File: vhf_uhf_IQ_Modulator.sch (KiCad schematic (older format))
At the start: 28 parts

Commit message: Adding docks and details in diagram
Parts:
- added C? (x2): 10uF 16V, symbol CP_Small
- added C? (x2): CP_Small, symbol CP_Small
- added C? (x4): 2200pF, symbol C_Small
- added J?: Audio-Jack-3, symbol Audio-Jack-3
- added R? (x4): 1K, symbol R
- added RV? (x2): 4k7, symbol POT
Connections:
- wire segments 74 -> 107
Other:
- note added: "1200pF / fc= 132KHz\n2200pF / fc=72KHz\n3300pF / fc=48KHz\n4700pF / fc=34KHz"
- note added: "27dBm 500 mW (max)"
- note added: "Check Volatge"
- moved on the sheet: C?, F?, J?, R?, U?

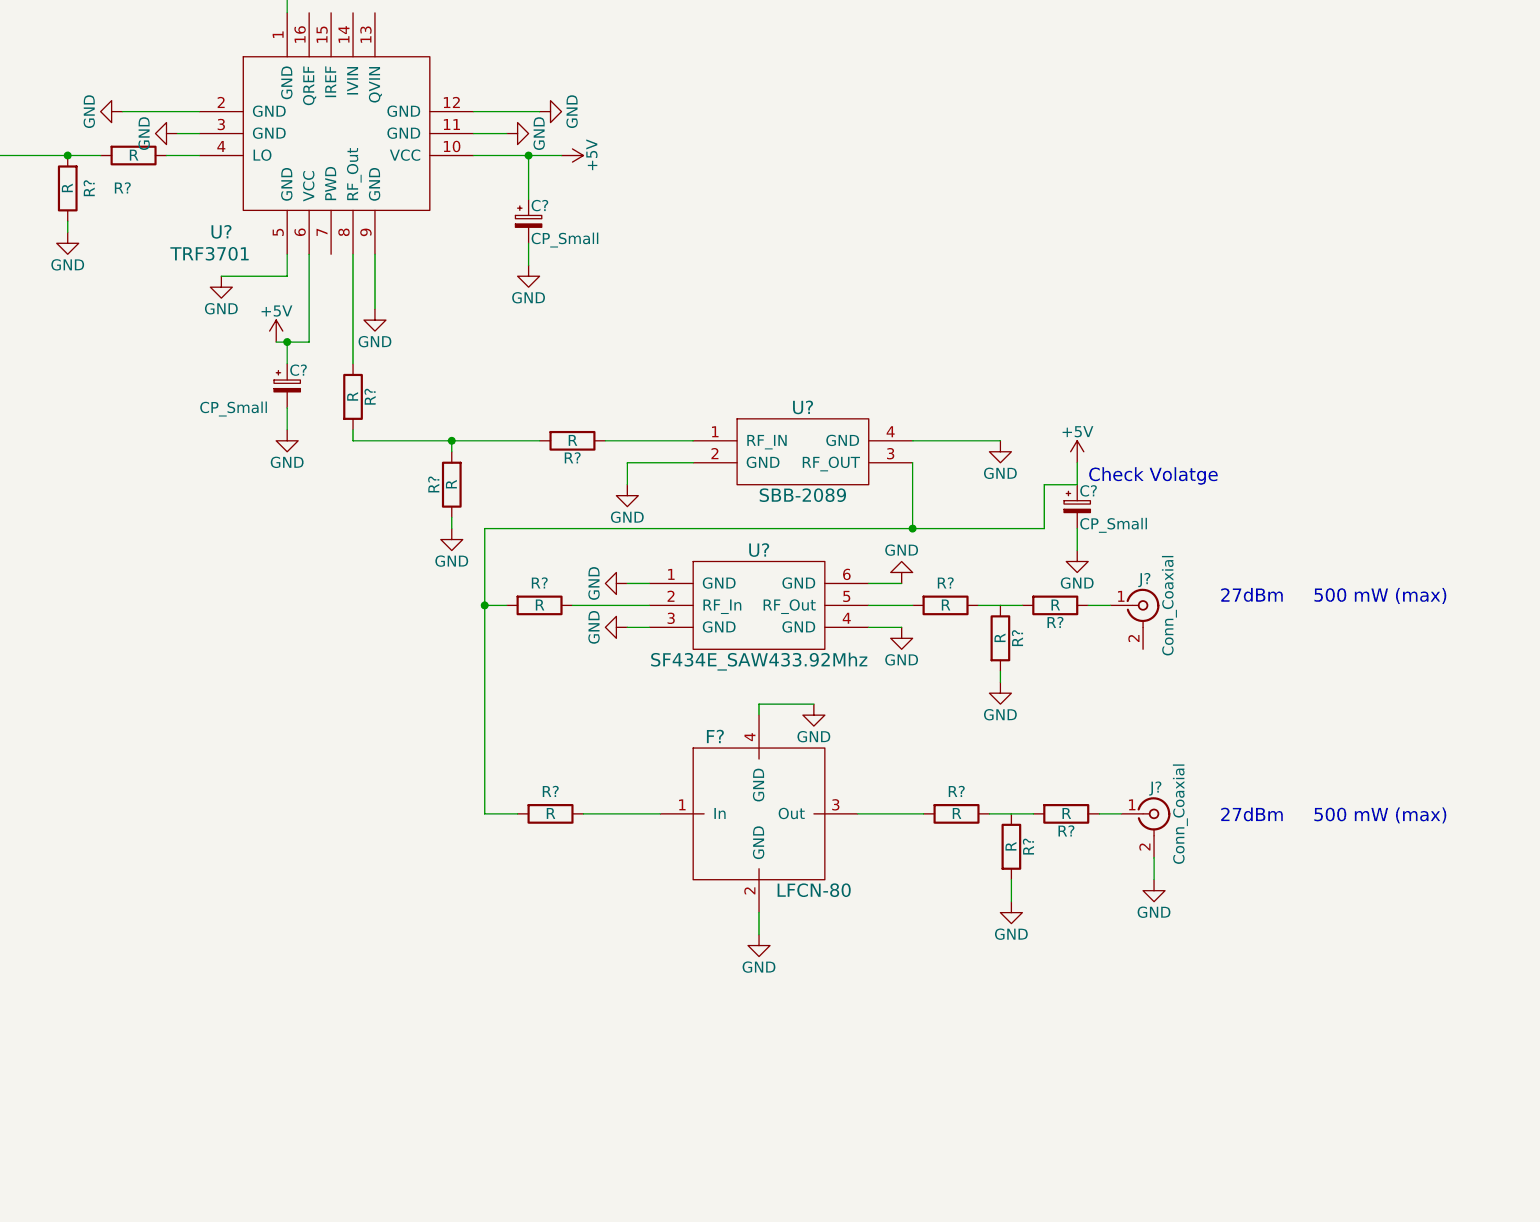
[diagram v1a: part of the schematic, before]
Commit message: added rf switch
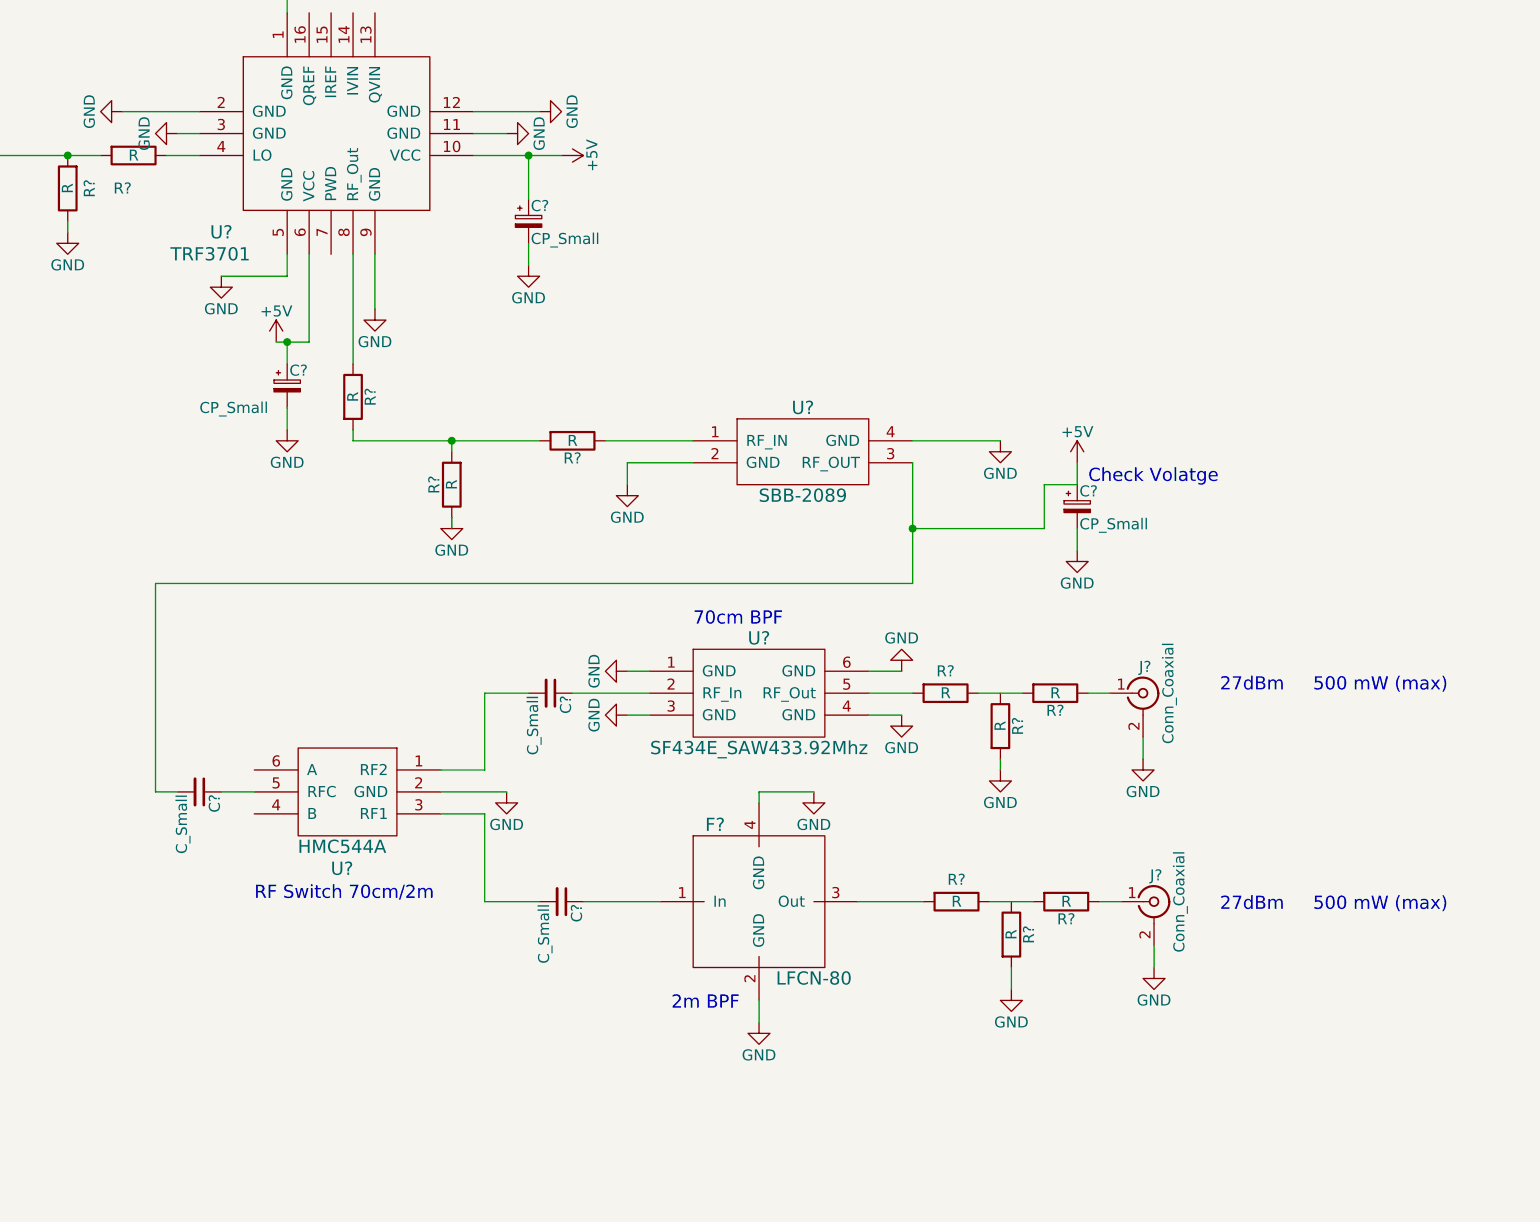
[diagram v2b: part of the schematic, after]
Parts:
- removed R? (x2): R, symbol R
- added C? (x3): C_Small, symbol C_Small
- added U?: HMC544A, symbol HMC544A
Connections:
- wire segments 107 -> 116
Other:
- note added: "2m BPF"
- note added: "70cm BPF"
- note added: "RF Switch 70cm/2m"
- moved on the sheet: F?, J?, R?, U?

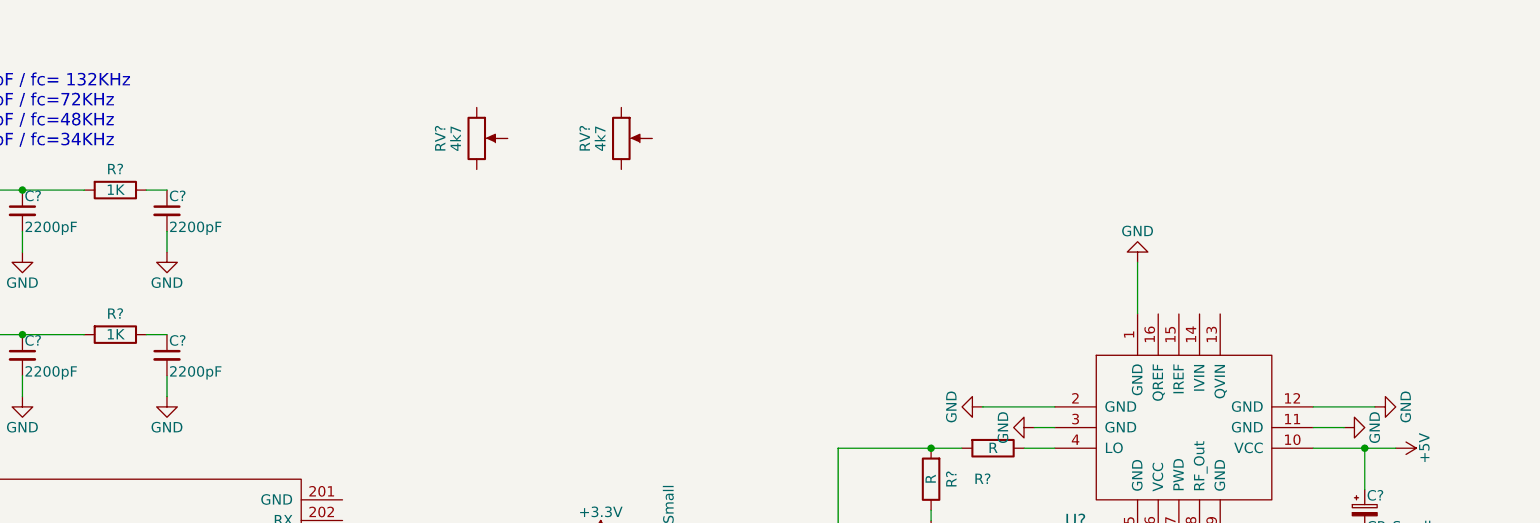
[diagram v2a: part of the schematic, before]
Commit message: added i and q ref voltage
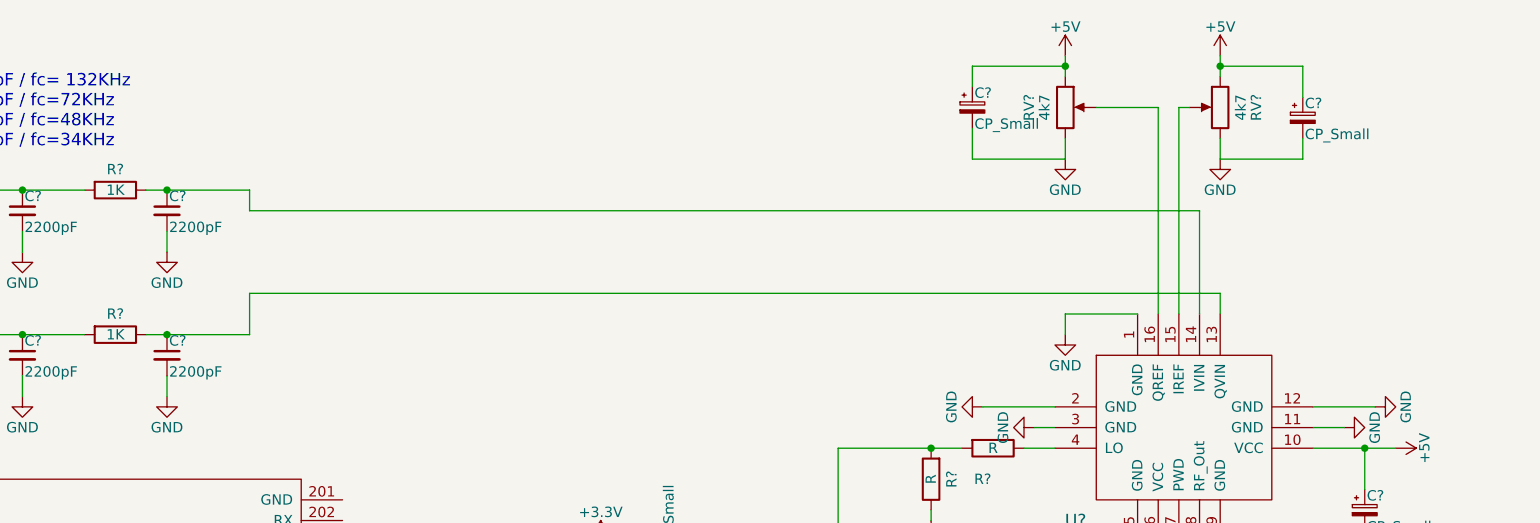
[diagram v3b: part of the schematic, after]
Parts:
- added C? (x2): CP_Small, symbol CP_Small
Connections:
- wire segments 116 -> 139
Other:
- moved on the sheet: RV?
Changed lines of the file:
@@
 L GND #PWR?
 U 1 1 59FF3FE4
-P 7700 1650
-F 0 "#PWR?" H 7700 1400 50  0001 C CNN
-F 1 "GND" H 7700 1500 50  0000 C CNN
-F 2 "" H 7700 1650 50  0001 C CNN
-F 3 "" H 7700 1650 50  0001 C CNN
-	1    7700 1650
-	-1   0    0    1
+P 7350 2000
+F 0 "#PWR?" H 7350 1750 50  0001 C CNN
+F 1 "GND" H 7350 1850 50  0000 C CNN
+F 2 "" H 7350 2000 50  0001 C CNN
+F 3 "" H 7350 2000 50  0001 C CNN
+	1    7350 2000
+	1    0    0    -1
 $EndComp
 $Comp
@@
 	1450 8550 700  8550
 Wire Wire Line
-	7700 1650 7700 1900
-Wire Wire Line
 	8100 3000 8100 3250
 Wire Wire Line
@@
 Connection ~ 2300 1300
 Wire Wire Line
-	3000 1300 2900 1300
-Wire Wire Line
 	2300 1500 2300 1600
 Wire Wire Line
@@
 Connection ~ 2300 2000
 Wire Wire Line
-	3000 2000 2900 2000
+	2900 2000 3400 2000
 Wire Wire Line
 	2300 2200 2300 2300
@@
 L POT RV?
 U 1 1 5A147320
-P 4500 1050
-F 0 "RV?" V 4325 1050 50  0000 C CNN
-F 1 "4k7" V 4400 1050 50  0000 C CNN
-F 2 "" H 4500 1050 50  0001 C CNN
-F 3 "" H 4500 1050 50  0001 C CNN
-	1    4500 1050
-	1    0    0    -1
+P 8100 900
+F 0 "RV?" V 7925 900 50  0000 C CNN
+F 1 "4k7" V 8000 900 50  0000 C CNN
+F 2 "" H 8100 900 50  0001 C CNN
+F 3 "" H 8100 900 50  0001 C CNN
+	1    8100 900
+	-1   0    0    -1
 $EndComp
 $Comp
 L POT RV?
 U 1 1 5A1473F1
-P 5200 1050
-F 0 "RV?" V 5025 1050 50  0000 C CNN
-F 1 "4k7" V 5100 1050 50  0000 C CNN
-F 2 "" H 5200 1050 50  0001 C CNN
-F 3 "" H 5200 1050 50  0001 C CNN
-	1    5200 1050
+P 7350 900
+F 0 "RV?" V 7175 900 50  0000 C CNN
+F 1 "4k7" V 7250 900 50  0000 C CNN
+F 2 "" H 7350 900 50  0001 C CNN
+F 3 "" H 7350 900 50  0001 C CNN
+	1    7350 900
 	1    0    0    -1
 $EndComp
@@
 Wire Wire Line
 	8400 5450 8700 5450
+Wire Wire Line
+	7950 900  7900 900
+Wire Wire Line
+	7900 900  7900 1900
+Wire Wire Line
+	7800 1900 7800 900
+Wire Wire Line
+	7800 900  7500 900
+$Comp
+L GND #PWR?
+U 1 1 5A1CAF8C
+P 8100 1150
+F 0 "#PWR?" H 8100 900 50  0001 C CNN
+F 1 "GND" H 8100 1000 50  0000 C CNN
+F 2 "" H 8100 1150 50  0001 C CNN
+F 3 "" H 8100 1150 50  0001 C CNN
+	1    8100 1150
+	1    0    0    -1
+$EndComp
+$Comp
+L GND #PWR?
+U 1 1 5A1CB01E
+P 7350 1150
+F 0 "#PWR?" H 7350 900 50  0001 C CNN
+F 1 "GND" H 7350 1000 50  0000 C CNN
+F 2 "" H 7350 1150 50  0001 C CNN
+F 3 "" H 7350 1150 50  0001 C CNN
+	1    7350 1150
+	1    0    0    -1
+$EndComp
+$Comp
+L +5V #PWR?
+U 1 1 5A1CB0DD
+P 8100 650
+F 0 "#PWR?" H 8100 500 50  0001 C CNN
+F 1 "+5V" H 8100 790 50  0000 C CNN
+F 2 "" H 8100 650 50  0001 C CNN
+F 3 "" H 8100 650 50  0001 C CNN
+	1    8100 650
+	1    0    0    -1
+$EndComp
+$Comp
+L +5V #PWR?
+U 1 1 5A1CB1C9
+P 7350 650
+F 0 "#PWR?" H 7350 500 50  0001 C CNN
+F 1 "+5V" H 7350 790 50  0000 C CNN
+F 2 "" H 7350 650 50  0001 C CNN
+F 3 "" H 7350 650 50  0001 C CNN
+	1    7350 650
+	1    0    0    -1
+$EndComp
+Wire Wire Line
+	7350 650  7350 750
+Wire Wire Line
+	8100 650  8100 750
+$Comp
+L CP_Small C?
+U 1 1 5A1CB46E
+P 8500 950
+F 0 "C?" H 8510 1020 50  0000 L CNN
+F 1 "CP_Small" H 8510 870 50  0000 L CNN
+F 2 "" H 8500 950 50  0001 C CNN
+F 3 "" H 8500 950 50  0001 C CNN
+	1    8500 950
+	1    0    0    -1
+$EndComp
+$Comp
+L CP_Small C?
+U 1 1 5A1CB572
+P 6900 900
+F 0 "C?" H 6910 970 50  0000 L CNN
+F 1 "CP_Small" H 6910 820 50  0000 L CNN
+F 2 "" H 6900 900 50  0001 C CNN
+F 3 "" H 6900 900 50  0001 C CNN
+	1    6900 900
+	1    0    0    -1
+$EndComp
+Wire Wire Line
+	7350 700  6900 700
+Wire Wire Line
+	6900 700  6900 800
+Connection ~ 7350 700
+Wire Wire Line
+	7350 1150 6900 1150
+Wire Wire Line
+	6900 1150 6900 1000
+Wire Wire Line
+	7350 1050 7350 1150
+Wire Wire Line
+	8500 850  8500 700
+Wire Wire Line
+	8500 700  8100 700
+Connection ~ 8100 700
+Wire Wire Line
+	8500 1050 8500 1150
+Wire Wire Line
+	8500 1150 8100 1150
+Wire Wire Line
+	8100 1150 8100 1050
+Wire Wire Line
+	7700 1900 7350 1900
+Wire Wire Line
+	7350 1900 7350 2000
+Connection ~ 3000 1300
+Wire Wire Line
+	8100 1900 8100 1800
+Wire Wire Line
+	8100 1800 3400 1800
+Wire Wire Line
+	3400 1800 3400 2000
+Connection ~ 3000 2000
+Wire Wire Line
+	8000 1900 8000 1400
+Wire Wire Line
+	8000 1400 3400 1400
+Wire Wire Line
+	3400 1300 3400 1400
+Wire Wire Line
+	2900 1300 3400 1300
 $EndSCHEMATC

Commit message: added power and usb
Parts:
- added J?: USB3_A, symbol USB3_A
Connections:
- wire segments 139 -> 152
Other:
- moved on the sheet: C?, F?, J?, R?, RV?, U?

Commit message: added dokuments
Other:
- note added: "-3dBm"
- note added: "27dB gain"
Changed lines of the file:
@@
 LIBS:contrib
 LIBS:valves
+LIBS:RFSolutions
 LIBS:Oscillators
 LIBS:microchip_pic32mcu
@@
 Wire Wire Line
 	9150 5400 9150 5350
+Text Notes 12900 4300 0    60   ~ 0
+-3dBm
+Text Notes 14600 4250 0    60   ~ 0
+27dB gain
 $EndSCHEMATC

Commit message: Added real time clock
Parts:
- removed C?: C_Small, symbol C_Small
- removed J?: RPi_GPIO, symbol RPi_GPIO
- added BT?: 3.3V Battery_Cell, symbol Battery_Cell
- added C? (x11): C_Small, symbol C_Small
- added C?: 22pF, symbol C
- added C?: 100nF, symbol C
- added D?: 1N4148, symbol D
- added L? (x5): L, symbol L
- added R? (x2): R, symbol R
- added R?: 56, symbol R
- added R? (x2): 4k7, symbol R
- added U?: 74AHC1G04, symbol 74AHC1G04
- added U?: PCF8563, symbol PCF8563
- added U?: MMZ09332BT1, symbol MMZ09332BT1
- added Y?: 32.768Khz, symbol Crystal
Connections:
- net labels added: INT, PDet, SCL, SDA
- wire segments 152 -> 199
- no-connect marks 0 -> 1
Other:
- note added: "RTC"
- note removed: "-3dBm"
- note removed: "27dB gain"
- moved on the sheet: C?, F?, J?, R?, RV?, U?
